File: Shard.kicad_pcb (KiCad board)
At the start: 4 copper layers, 52 parts, among them J1 USB_C_Receptacle_USB2.0_16P, J2 Conn_01x08, J3 Conn_01x08, J4 Conn_01x08, J5 Conn_01x08, SW1 SW_Push, SW2 SW_Push, U1 ESP32-S3, U2 USBLC6-2P6, U3 TLV76733DRVx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

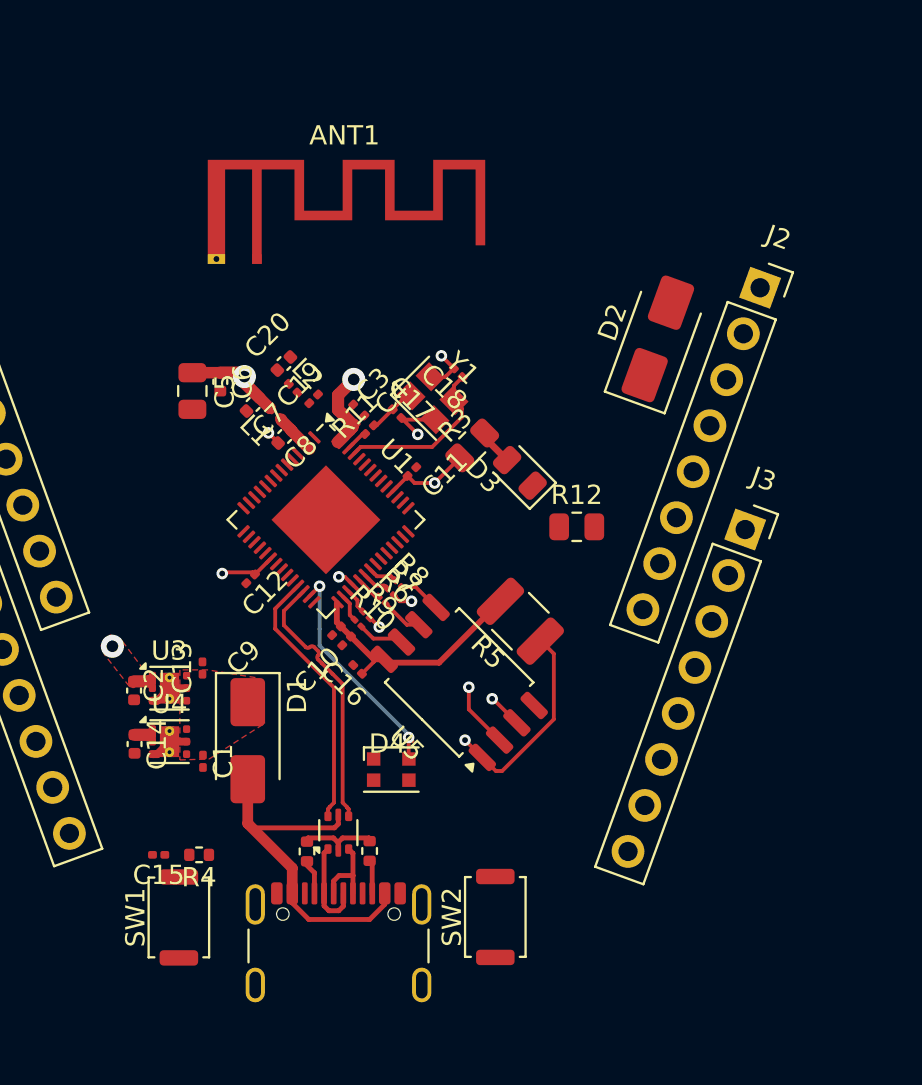
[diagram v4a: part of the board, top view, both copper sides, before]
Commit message: RF routing and impedence matching
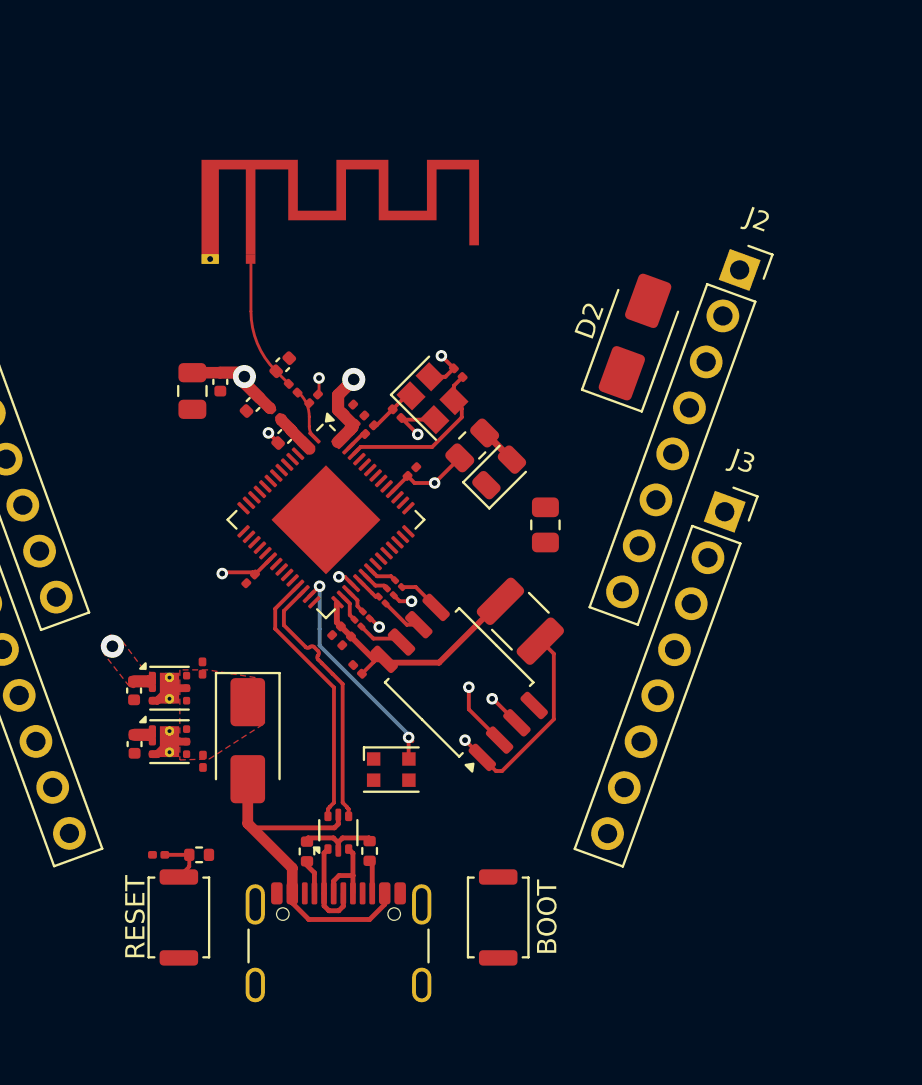
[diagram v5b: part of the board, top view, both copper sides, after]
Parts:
- moved R12 1.63 mm to (157.9, 94.0), turned to 90 degrees
- moved J3 1.41 mm to (167.3, 93.3)
- moved J2 1.41 mm to (168.0, 80.8)
- moved D2 1.19 mm to (162.6, 84.3)
- moved D3 1.08 mm to (155.6, 91.3), turned to 45 degrees
- moved ANT1 0.32 mm to (142.7, 80.2)
- moved BOOT 0.15 mm to (155.5, 114.4)
- moved C20 0.09 mm to (144.3, 85.7)
- renumbered SW2 to BOOT, SW1 to RESET
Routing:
- net Net-(ANT1-Pad1): track 0.00 -> 6.81 mm
- net /LNA_IN: track 0.00 -> 2.67 mm
- net /RESET: track 0.00 -> 2.64 mm
- net +3.3V: track 49.2 -> 50.1 mm
- net GND: track 14.9 -> 15.8 mm, vias 3 -> 4

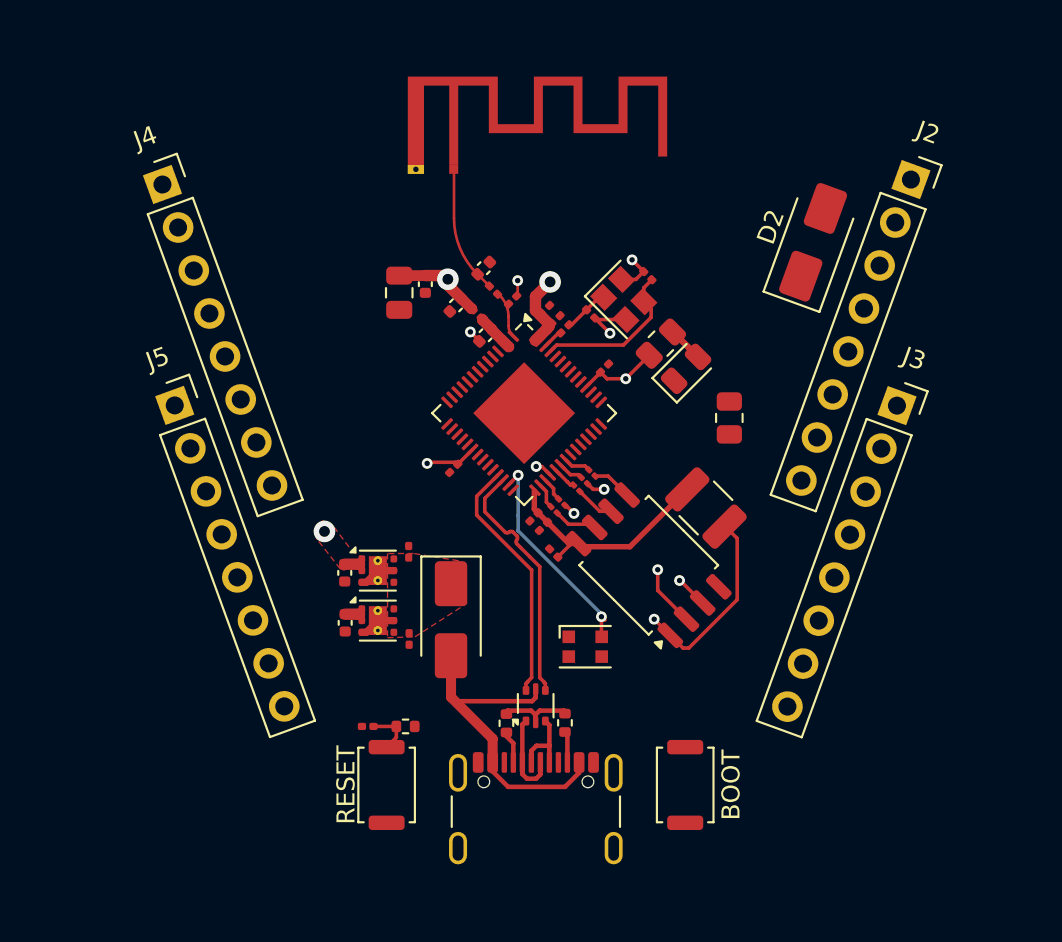
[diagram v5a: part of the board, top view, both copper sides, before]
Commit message: Routed most GPIO pins
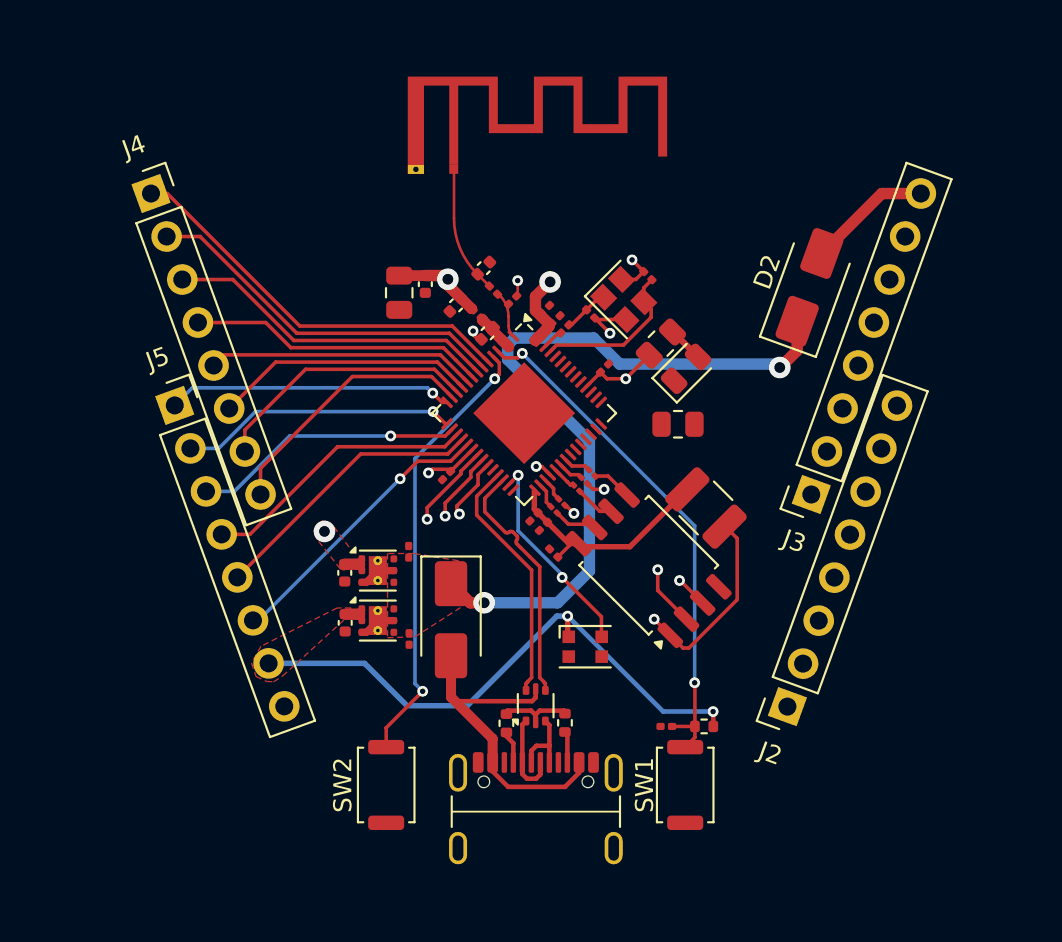
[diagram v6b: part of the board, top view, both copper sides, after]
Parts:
- moved J2 30.1 mm to (161.2, 110.0), turned to 160 degrees
- moved SW2 16.6 mm to (138.9, 114.4)
- moved R4 16.6 mm to (156.6, 111.2)
- moved C15 16.6 mm to (154.4, 111.2)
- moved SW1 16.6 mm to (155.5, 114.4)
- moved J3 6.85 mm to (162.5, 98.3), turned to 160 degrees
- moved R12 2.87 mm to (155.1, 94.4), turned to 0 degrees
- moved D2 2.51 mm to (162.4, 86.8)
- moved J4 0.81 mm to (125.8, 81.6)
- moved C12 0.56 mm to (142.3, 97.2)
- moved C8 0.16 mm to (144.5, 89.3)
- renumbered RESET to SW1, BOOT to SW2
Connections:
- J2 pad 1: /1 -> /15
- J2 pad 2: /2 -> /16
- J2 pad 3: /3 -> /17
- J2 pad 4: /4 -> /18
- J2 pad 5: /5 -> /21
- J2 pad 6: /6 -> /38
- J2 pad 7: /7 -> /47
- J2 pad 8: /8 -> /48
- J3 pad 1: /9 -> /RX
- J3 pad 2: /10 -> /TX
- J3 pad 3: /11 -> /RESET
- J3 pad 4: /12 -> GND
- J3 pad 5: /13 -> GND
- J3 pad 6: /14 -> GND
- J3 pad 7: /15 -> /E3.3V
- J3 pad 8: GND -> Net-(D2-A)
- J4 pad 1: /16 -> /1
- J4 pad 2: /17 -> /2
- J4 pad 3: /18 -> /3
- J4 pad 4: /21 -> /4
- J4 pad 5: /38 -> /5
- J4 pad 6: /47 -> /6
- J4 pad 7: /48 -> /7
- J4 pad 8: GND -> /8
- J5 pad 1: Net-(D2-A) -> /9
- J5 pad 2: /RESET -> /10
- J5 pad 3: /RX -> /11
- J5 pad 4: /TX -> /12
- J5 pad 5: GND -> /13
- J5 pad 6: GND -> /14
- J5 pad 7: GND -> /E3.3V
- J5 pad 8: /E3.3V -> GND
- R4 pad 1: +3.3V -> /E3.3V
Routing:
- net /E3.3V: track 1.45 -> 79.1 mm, vias 0 -> 2
- net /VIN: track 0.00 -> 42.2 mm, vias 0 -> 2
- net /15: track 0.00 -> 29.1 mm, vias 0 -> 1
- net /16: track 0.00 -> 27.3 mm, vias 0 -> 1
- net /17: track 0.00 -> 26.3 mm, vias 0 -> 1
- net /RESET: track 2.64 -> 28.9 mm, vias 0 -> 2
- net /BOOT: track 0.00 -> 24.8 mm, vias 0 -> 2
- net /1: track 0.00 -> 22.6 mm
- net /2: track 0.00 -> 20.5 mm
- net /3: track 0.00 -> 18.5 mm
- net /4: track 0.00 -> 16.5 mm
- net /14: track 0.00 -> 16.0 mm, vias 0 -> 1
- net /9: track 0.00 -> 15.9 mm, vias 0 -> 1
- net /13: track 0.00 -> 15.7 mm
- net /12: track 0.00 -> 15.4 mm
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- added copper zone on F.Cu, net /E3.3V

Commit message: Finished routing
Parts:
- moved D3 4.25 mm to (155.1, 95.5), turned to 180 degrees
- moved R12 4.25 mm to (157.2, 90.7), turned to -45 degrees
- moved R3 3.04 mm to (154.4, 92.9), turned to -90 degrees
- moved C11 0.59 mm to (151.1, 91.8), turned to -45 degrees
- moved U5 0.16 mm to (153.5, 102.4)
- moved C16 0.10 mm to (148.2, 101.6)
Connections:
- J2 pad 5: /21 -> GND
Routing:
- net /RX: track 0.00 -> 24.6 mm, vias 0 -> 2
- net /18: track 0.00 -> 22.6 mm, vias 0 -> 1
- net /47: track 0.00 -> 19.3 mm, vias 0 -> 1
- net /48: track 0.00 -> 19.2 mm, vias 0 -> 1
- net /38: track 0.11 -> 16.9 mm
- net /RESET: track 28.9 -> 43.8 mm, vias 2 -> 3
- net /VIN: track 42.2 -> 33.2 mm
- net Net-(U1-U0TXD): track 0.00 -> 8.01 mm
- net /TX: track 0.00 -> 7.41 mm, vias 0 -> 2
- net +3.3V: track 52.4 -> 56.6 mm
- net /E3.3V: track 79.1 -> 83.0 mm
- net /15: track 29.1 -> 31.4 mm
- net /SPICS0: track 23.2 -> 21.7 mm
- net /21: track 11.4 -> 10.7 mm
- net GND: vias 4 -> 9

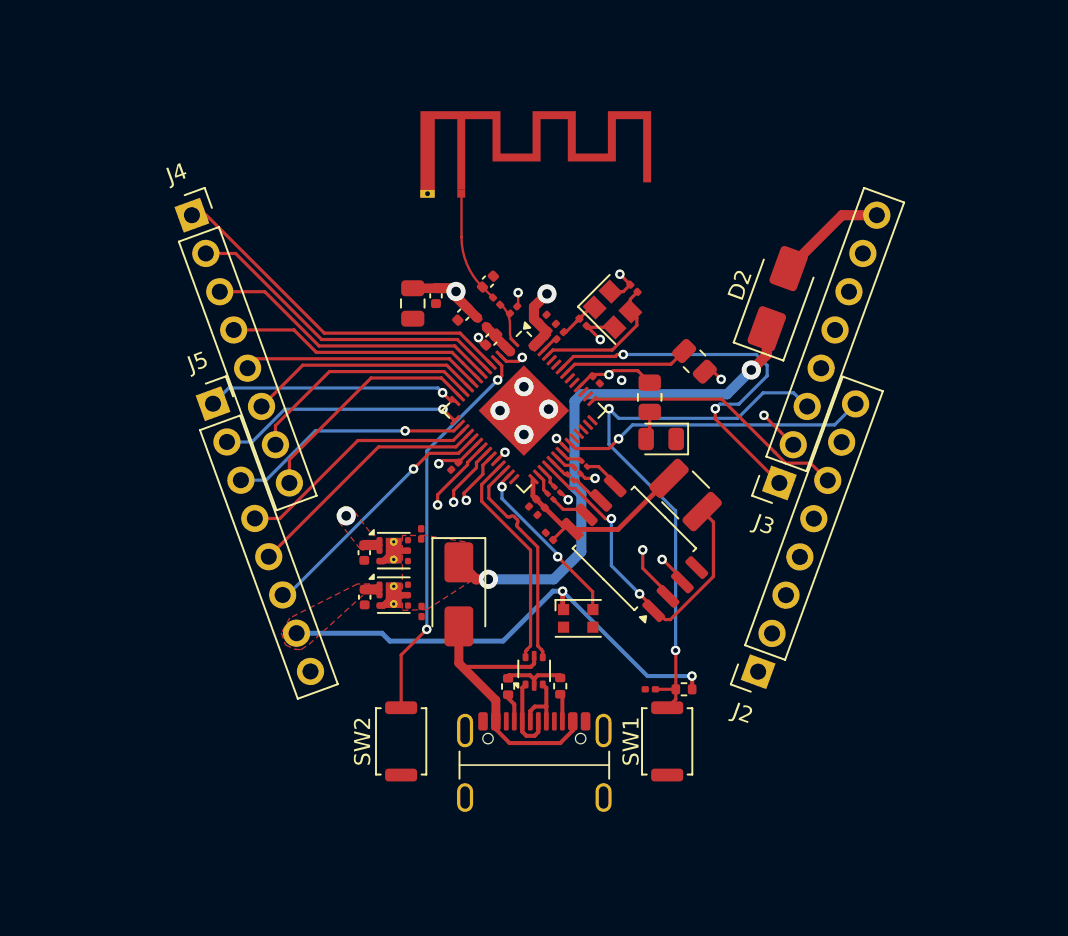
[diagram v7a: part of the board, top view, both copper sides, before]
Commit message: Add PCB margin
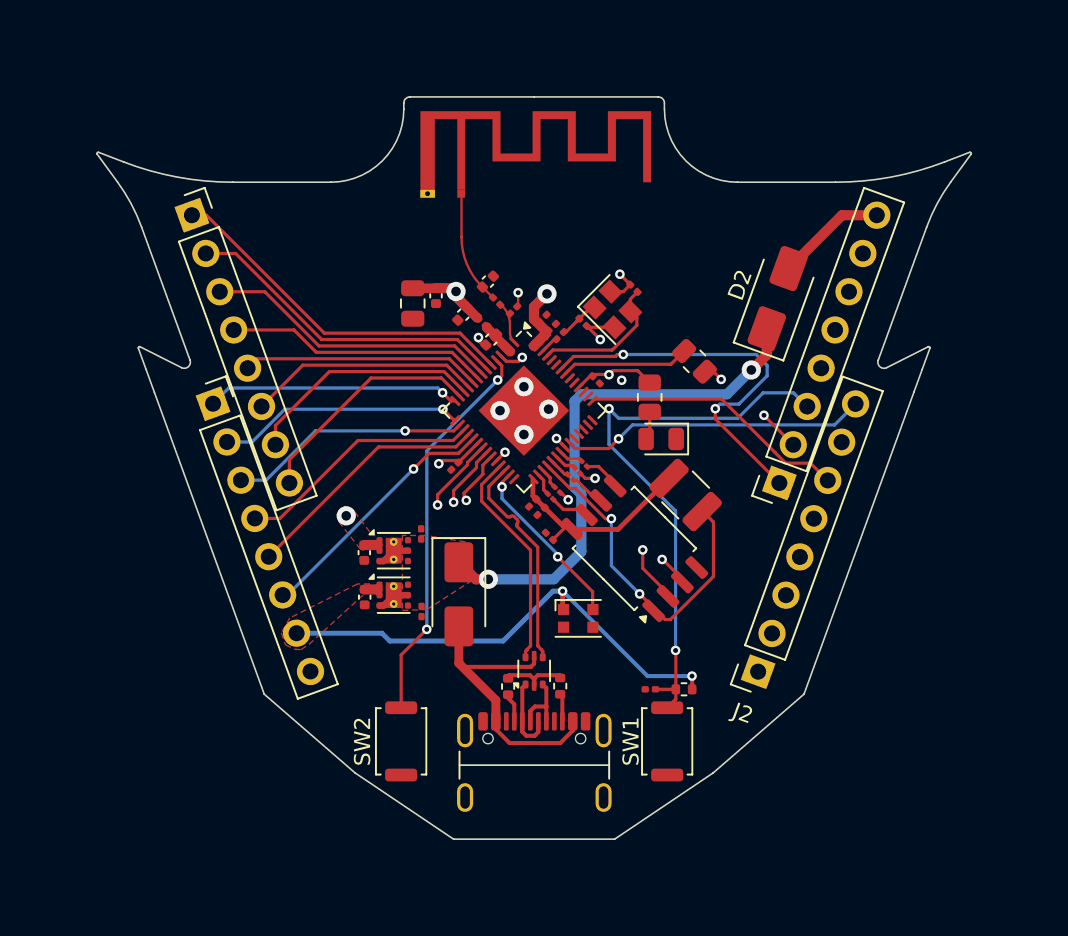
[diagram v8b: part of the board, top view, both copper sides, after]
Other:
- board outline added: 54.6 x 46.3 mm
